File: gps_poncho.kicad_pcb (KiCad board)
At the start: 2 copper layers, 86.4 x 61 mm, 7 parts, among them P1 CONN_5, P2 CONN_4

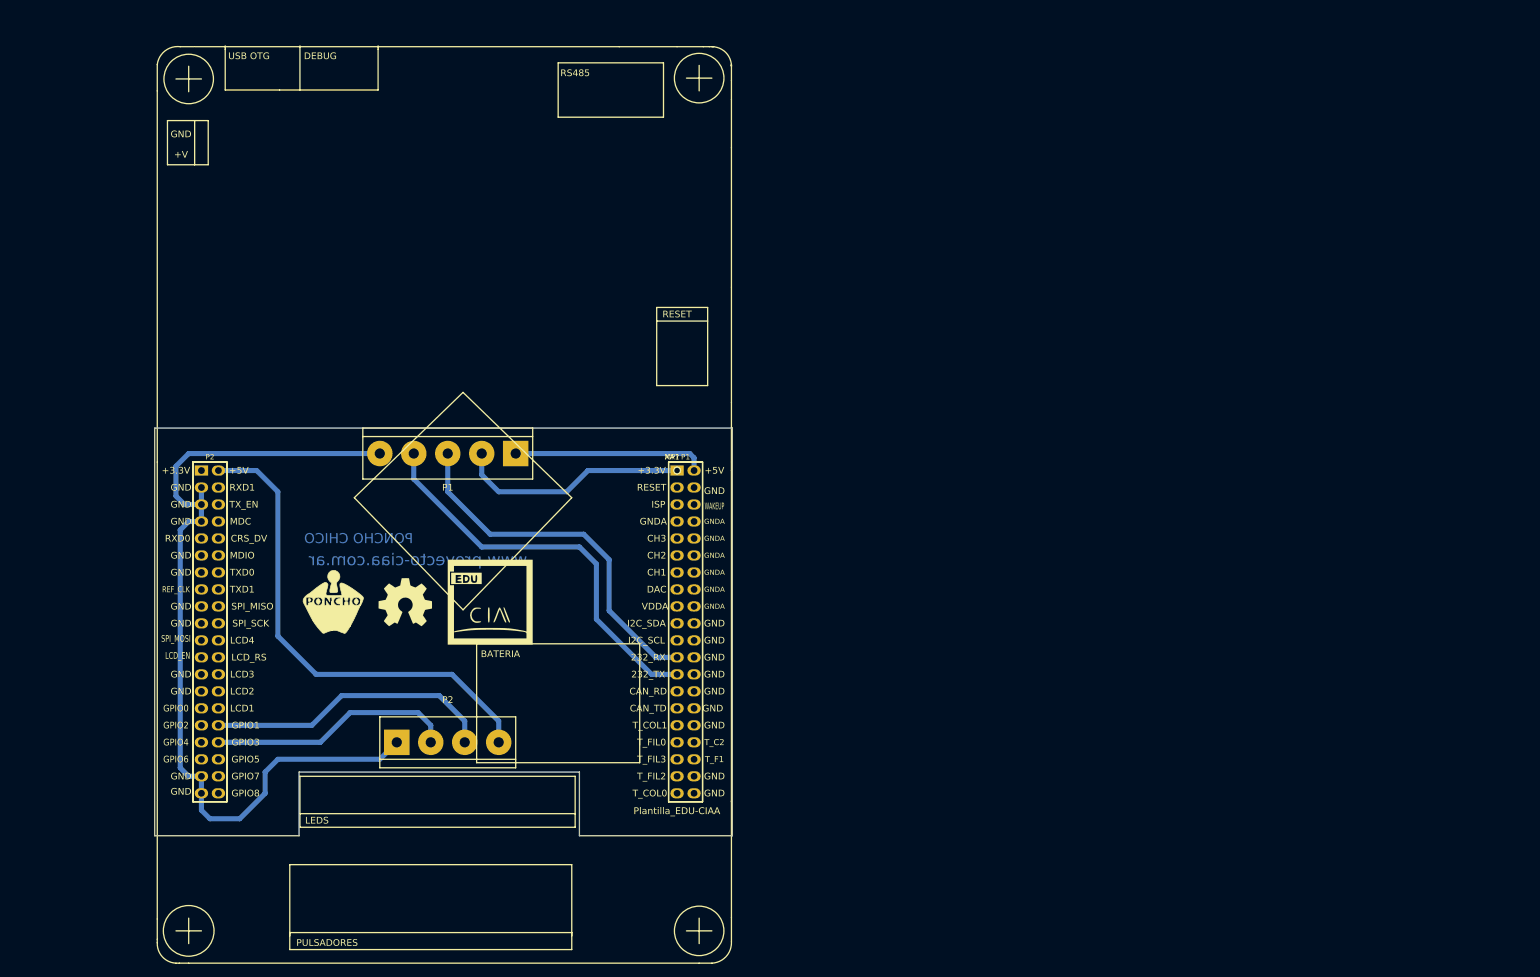
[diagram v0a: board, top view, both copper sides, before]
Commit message: Cambio de modelo de poncho inicial: Uso modelo Basico
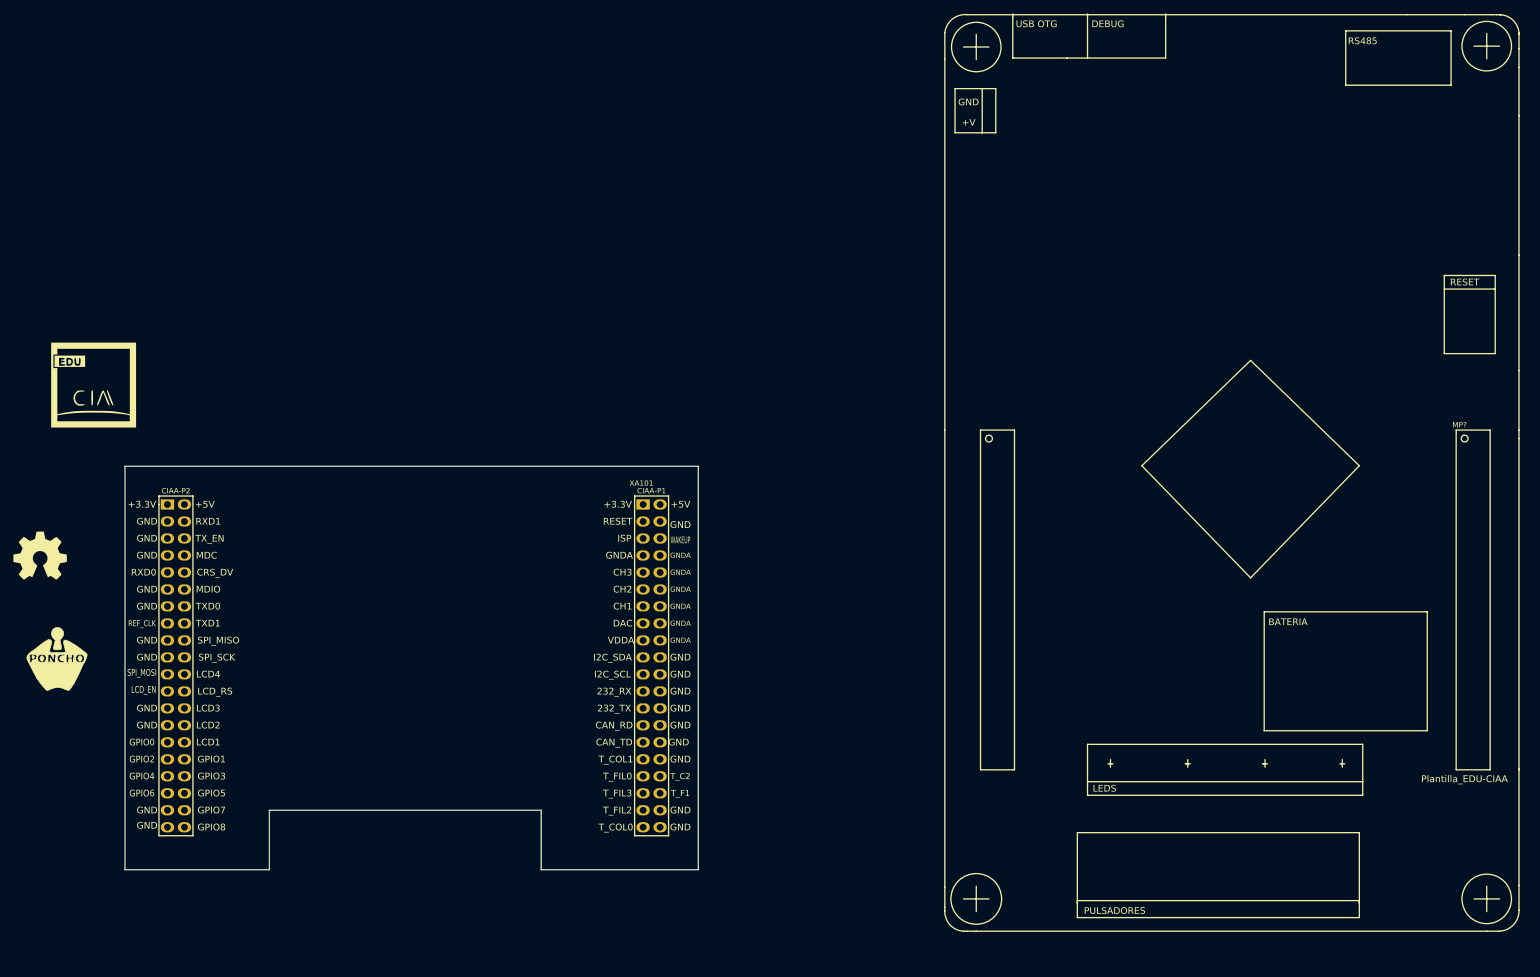
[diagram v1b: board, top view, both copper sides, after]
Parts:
- removed the G*** at (114.3, 101.0)
- removed the G*** at (90.8, 101.0)
- removed the MP? at (142.2, 81.3)
- removed P1: CONN_5, Poncho_Modelos:bornier5
- removed P2: CONN_4, Poncho_Modelos:bornier4
- removed XA1: Conn_PonchoMP_2x_20x2, Poncho_Esqueleto:Conn_Poncho_Chico
- added G***: Logo_EDU-CIAA, footprint:Logo_EDU-CIAA, F.Cu at (55.0, 68.5)
- added G***: LOGO, footprint:Logo_Poncho, F.Cu at (49.5, 109.5)
- added MP?: Plantilla_EDU-CIAA, footprint:Plantilla_EDU-CIAA, F.Cu at (260.0, 76.5)
- added XA101: Conn_Poncho2P_2x_20x2, footprint:Conn_Poncho_SinBorde, F.Cu at (137.2, 86.4)
- G101: footprint Poncho_Esqueleto:Logo_OSHWA -> footprint:Logo_OSHWA
- moved G101 55.0 mm to (47.0, 94.0)
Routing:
- net GND: track 130.8 -> 0.00 mm
- net +5VP: track 73.3 -> 0.00 mm
- net Net-(P1-Pad4): track 60.1 -> 0.00 mm
- net Net-(P1-Pad3): track 54.7 -> 0.00 mm
- net Net-(P2-Pad3): track 43.4 -> 0.00 mm
- net Net-(P2-Pad2): track 36.9 -> 0.00 mm
- net +3.3V: track 34.8 -> 0.00 mm
- net +5V: track 28.8 -> 0.00 mm
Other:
- board size 86.4 x 61 mm -> 85.7 x 60.3 mm
- net class Default: clearance 0.508 -> 0.51
- rule trace_clearance: 0.508 -> 0.51
- board text added: "Editar este cuadro para reflejar cantidad de capas, si se han realizado cálculos de impedancia o si es relevante para el funcionamiento."
- board text added: "PONCHO BASICO http://www.proyecto-ciaa.com.ar/"
- board text added: "Se sugiere colocar Nombre de Poncho y autor en cobre, serigrafía y rótulo."
- board text removed: "Editar el stackup para reflejar cantidad de capas, si se han realizado cálculos de impedancia o si es relevante para el funcionamiento."
- board text removed: "PONCHO CHICO"
- board text removed: "PONCHO CHICO http://www.proyecto-ciaa.com.ar/"
- board text removed: "Para un diseño nuevo luego de modificar el esquemático: 1)Seleccionar el bloque del PCB y cotas. (click-drag-release). 2)Opción de borrar bloque (Botón derecho). 3)Marcar todo menos locked footprints (MP1 y XA1) 4) Aceptar. 5) Volver a cargar el netlist."
- board text removed: "Se sugiere colocar código de Poncho en cobre, serigrafía y rótulo."
- board text removed: "www.proyecto-ciaa.com.ar"
